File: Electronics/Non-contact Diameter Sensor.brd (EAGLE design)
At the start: 45.4 x 55.2 mm, 11 parts

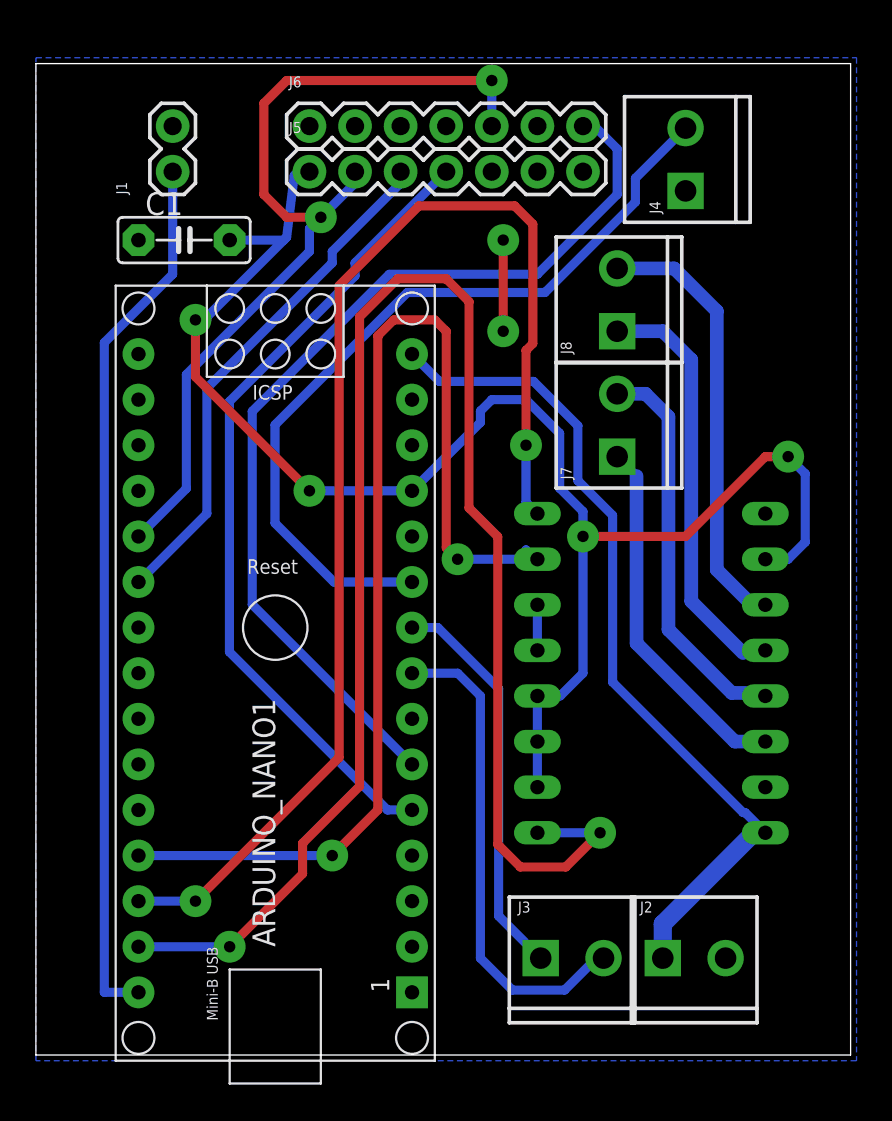
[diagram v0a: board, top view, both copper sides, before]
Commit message: Eliminated ground pour islands and reduced size of blank areas by moving traces. Moved J6 onto board a bit better.
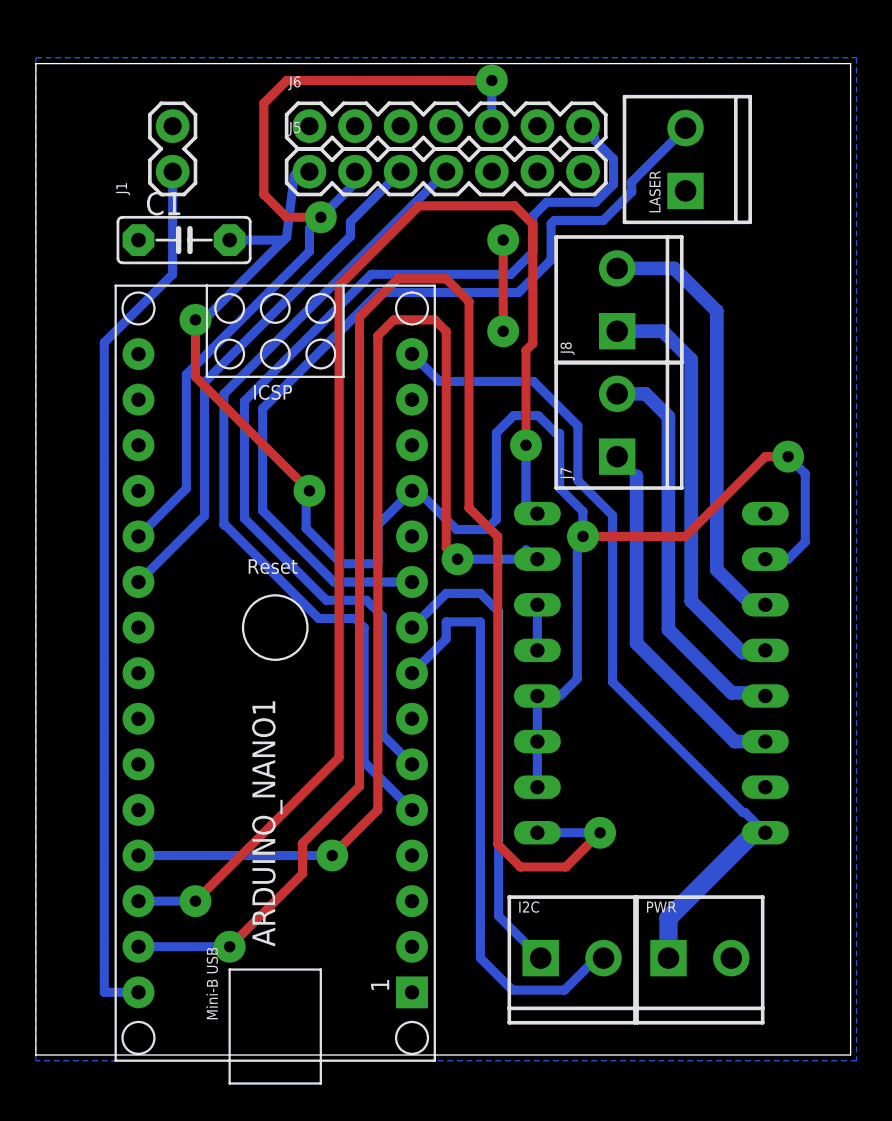
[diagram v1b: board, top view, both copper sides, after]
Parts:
- removed J2: (no value), SparkFun-Connectors:SCREWTERMINAL-3.5MM-2
- added PWR: (no value), SparkFun-Connectors:SCREWTERMINAL-3.5MM-2
- renumbered J3 to I2C, J4 to LASER
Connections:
- net 12V: now also PWR.1; no longer J2.1
- net GND: now also PWR.2; no longer J2.2
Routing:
- net 5V: track 87.7 -> 97.3 mm
- net SDA: track 27.3 -> 32.6 mm
- net SCL: track 22.2 -> 26.3 mm
- net AO2: track 53.7 -> 56.1 mm
- net LASER: track 45.0 -> 47.2 mm
- net AO1: track 45.6 -> 46.3 mm
- net CLK: track 28.9 -> 29.5 mm

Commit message: Redesigned the electronics board. Made the necessary changes in the pin assignments in the code. Updated image in the BOM.
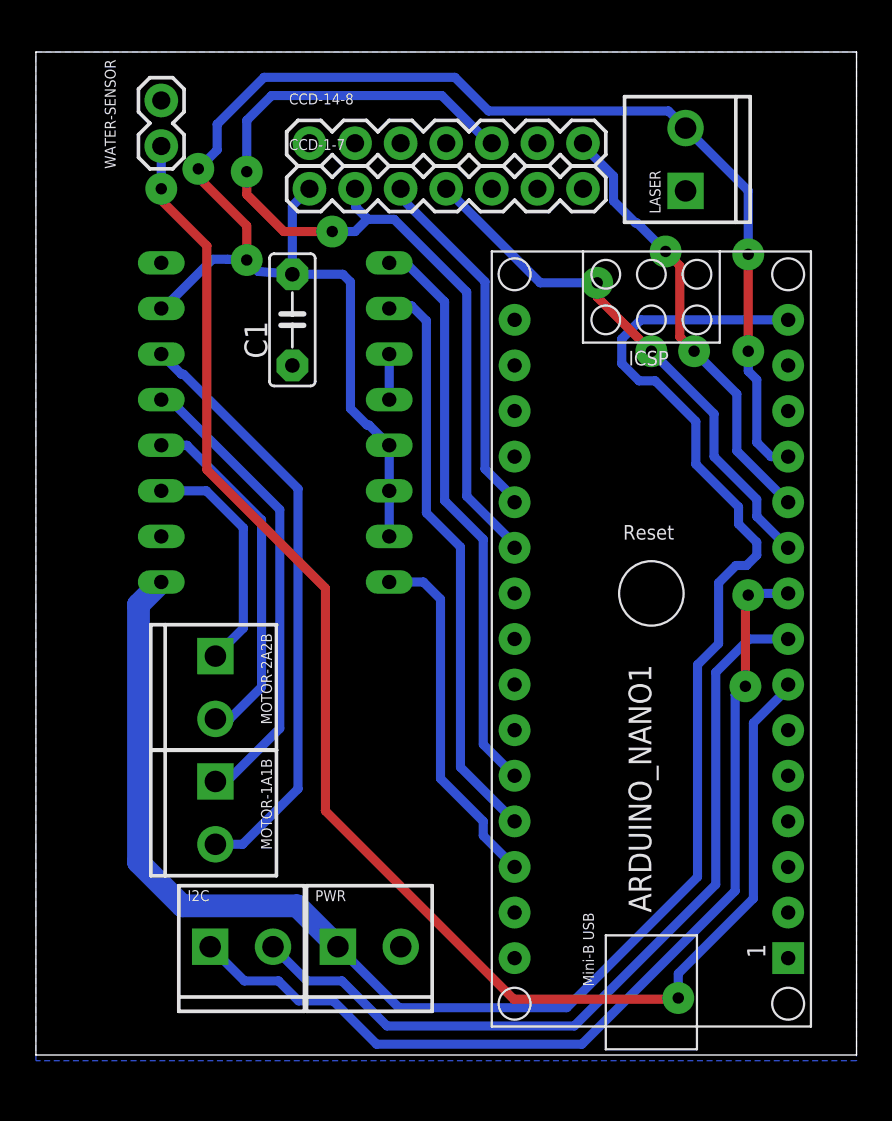
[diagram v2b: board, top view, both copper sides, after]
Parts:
- removed J1: (no value), SparkFun-Connectors:1X02
- removed J5, J6: (no value), SparkFun-Connectors:1X07
- removed J7, J8: (no value), SparkFun-Connectors:SCREWTERMINAL-3.5MM-2
- added CCD-1-7, CCD-14-8: (no value), SparkFun-Connectors:1X07
- added MOTOR-1A1B, MOTOR-2A2B: (no value), SparkFun-Connectors:SCREWTERMINAL-3.5MM-2
- added WATER-SENSOR: (no value), SparkFun-Connectors:1X02
- moved U$1 25.6 mm to (13.3, 35.2)
- moved ARDUINO_NANO1 21.0 mm to (34.3, 25.7)
- moved I2C 18.4 mm to (9.71, 6.03)
- moved PWR 18.4 mm to (16.8, 6.03)
- moved C1 7.49 mm to (14.3, 41.0), turned to 90 degrees
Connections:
- removed net LASER: ARDUINO_NANO1.10, LASER.2
- removed net WATER: ARDUINO_NANO1.30, J1.1
- new net N$1: ARDUINO_NANO1.7, WATER-SENSOR.1
- net 1A: now also MOTOR-1A1B.1; no longer J8.2
- net 1B: now also MOTOR-1A1B.2; no longer J8.1
- net 2A: now also MOTOR-2A2B.2; no longer J7.2
- net 2B: now also MOTOR-2A2B.1; no longer J7.1
- net 5V: now also CCD-1-7.1, LASER.2; no longer J5.1
- net AO1: now also ARDUINO_NANO1.10, CCD-1-7.4; no longer ARDUINO_NANO1.5, J5.4
- net AO2: now also ARDUINO_NANO1.11, CCD-14-8.7; no longer ARDUINO_NANO1.6, J6.7
- net CLK: now also ARDUINO_NANO1.20, CCD-1-7.3; no longer ARDUINO_NANO1.21, J5.3
- net DIRECTION: now also ARDUINO_NANO1.26; no longer ARDUINO_NANO1.28
- net ENABLE: now also ARDUINO_NANO1.28; no longer ARDUINO_NANO1.29
- net GND: now also CCD-1-7.5, CCD-14-8.3, WATER-SENSOR.2; no longer J1.2, J5.5, J6.3
- net SI1: now also ARDUINO_NANO1.21, CCD-1-7.2, CCD-14-8.5; no longer ARDUINO_NANO1.20, J5.2, J6.5
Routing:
- net N$1: track 0.00 -> 84.9 mm, vias 0 -> 2
- net ENABLE: track 92.1 -> 19.9 mm, vias 2 -> 0
- net 12V: track 47.8 -> 98.7 mm
- net WATER: track 49.2 -> 0.00 mm
- net LASER: track 47.2 -> 0.00 mm
- net DIRECTION: track 70.4 -> 32.2 mm, vias 2 -> 0
- net STEP: track 63.8 -> 32.4 mm, vias 2 -> 0
- net AO2: track 56.1 -> 24.8 mm, vias 0 -> 2
- net SCL: track 26.3 -> 54.1 mm, vias 0 -> 2
- net AO1: track 46.3 -> 29.8 mm, vias 0 -> 2
- net SDA: track 32.6 -> 46.4 mm
- net 1B: track 23.6 -> 33.3 mm
- net CLK: track 29.5 -> 20.1 mm
- net 2B: track 20.3 -> 13.2 mm
- net 5V: track 97.3 -> 91.1 mm
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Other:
- board size 45.4 x 55.2 mm -> 45.7 x 55.9 mm
